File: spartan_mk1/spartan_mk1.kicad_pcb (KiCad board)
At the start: 4 copper layers, 46.5 x 46.5 mm, 90 parts, among them J1 USB_B_Micro, J10 Conn_01x02_Female, J11 Conn_01x02_Female, J12 Conn_01x02_Female, J13 Conn_02x05_Odd_Even, J14 Conn_01x02_Female, J15 Conn_01x08_Female, J18 Conn_01x08_Female, J2 Conn_01x02_Female, J3 Conn_01x02_Female, J4 Conn_01x02_Female, J5 Conn_01x02_Female, J6 Conn_01x02_Female, J8 Conn_01x03_Female, J9 Conn_01x03_Female, Q1 2N7002, Q2 2N7002, Q3 AO3401A, SW1 SW_SPST, U1 MPU-6050, U2 AT24C256C-SSHL-T, U3 USBLC6-2SC6, U4 STM32F405RGTx, U5 AMS1117-3.3, U6 TPS5430DDA, Y1 X322516MLB4SI

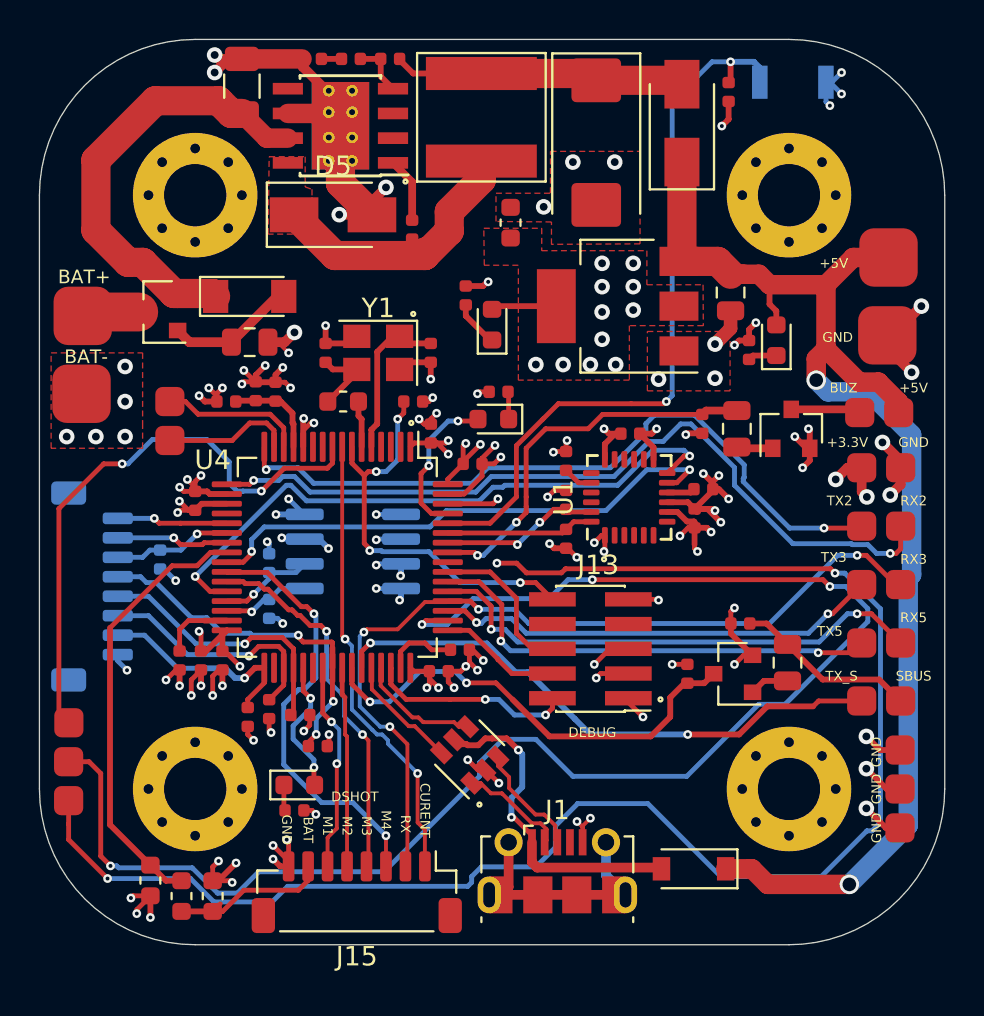
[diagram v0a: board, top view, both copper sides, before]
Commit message: Updated LED labels
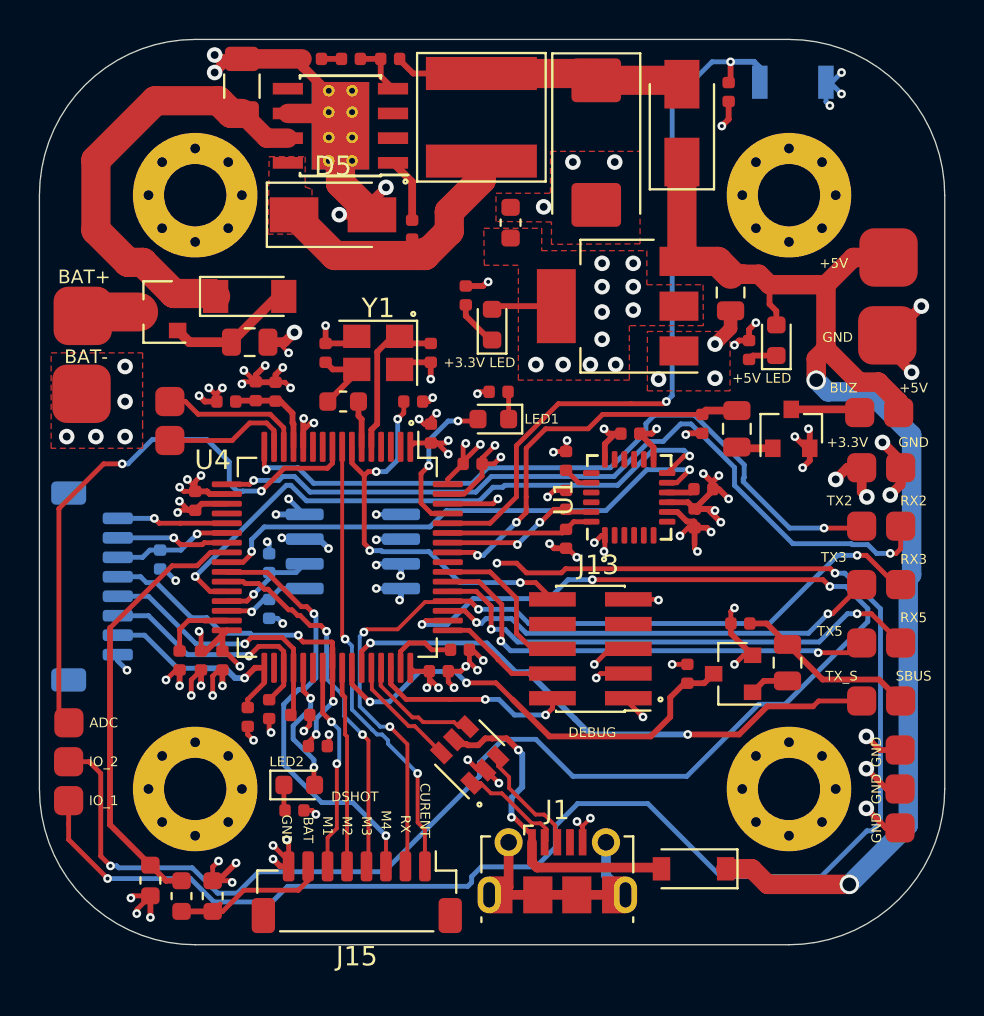
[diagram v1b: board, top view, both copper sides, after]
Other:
- board text added: "+3.3V LED"
- board text added: "+5V LED"
- board text added: "ADC"
- board text added: "IO_1"
- board text added: "IO_2"
- board text added: "LED1"
- board text added: "LED2"
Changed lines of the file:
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@@
   (general
     (thickness 1.6)
-    (drawings 54)
+    (drawings 61)
     (tracks 1230)
     (zones 0)
@@
     (46 B.CrtYd user)
     (47 F.CrtYd user)
-    (48 B.Fab user)
-    (49 F.Fab user)
+    (48 B.Fab user hide)
+    (49 F.Fab user hide)
   )
   (setup
@@
     )
   )
+  (gr_text LED2 (at 64.7 89.1) (layer F.SilkS)
+    (effects (font (size 0.5 0.5) (thickness 0.125)))
+  )
+  (gr_text LED1 (at 77.8 71.5) (layer F.SilkS)
+    (effects (font (size 0.5 0.5) (thickness 0.125)))
+  )
+  (gr_text "+3.3V LED" (at 74.6 68.6) (layer F.SilkS)
+    (effects (font (size 0.5 0.5) (thickness 0.125)))
+  )
+  (gr_text "+5V LED" (at 89.1 69.4) (layer F.SilkS)
+    (effects (font (size 0.5 0.5) (thickness 0.125)))
+  )
+  (gr_text IO_1 (at 55.3 91.1) (layer F.SilkS)
+    (effects (font (size 0.5 0.5) (thickness 0.125)))
+  )
+  (gr_text IO_2 (at 55.3 89.1) (layer F.SilkS)
+    (effects (font (size 0.5 0.5) (thickness 0.125)))
+  )
+  (gr_text ADC (at 55.3 87.1) (layer F.SilkS)
+    (effects (font (size 0.5 0.5) (thickness 0.125)))
+  )
   (gr_circle (center 83.9 85.9) (end 83.9 85.8) (layer F.SilkS) (width 0.12))
   (gr_circle (center 72.1 76.4) (end 72.2 76.4) (layer B.SilkS) (width 0.12))
@@
     (connect_pads (clearance 0.254))
     (min_thickness 0.254)
-    (fill yes (arc_segments 32) (thermal_gap 0.508) (thermal_bridge_width 0.508))
+    (fill (arc_segments 32) (thermal_gap 0.508) (thermal_bridge_width 0.508))
     (polygon
       (pts
@@
     (connect_pads (clearance 0.3))
     (min_thickness 0.254)
-    (fill yes (arc_segments 32) (thermal_gap 0.508) (thermal_bridge_width 0.508))
+    (fill (arc_segments 32) (thermal_gap 0.508) (thermal_bridge_width 0.508))
     (polygon
       (pts
@@
     (connect_pads (clearance 0.3))
     (min_thickness 0.254)
-    (fill yes (arc_segments 32) (thermal_gap 0.3) (thermal_bridge_width 2))
+    (fill (arc_segments 32) (thermal_gap 0.3) (thermal_bridge_width 2))
     (polygon
       (pts
@@
     (connect_pads (clearance 0.3))
     (min_thickness 0.254)
-    (fill yes (arc_segments 32) (thermal_gap 0.5) (thermal_bridge_width 0.5))
+    (fill (arc_segments 32) (thermal_gap 0.5) (thermal_bridge_width 0.5))
     (polygon
       (pts
@@
     (connect_pads (clearance 0.3))
     (min_thickness 0.254)
-    (fill yes (arc_segments 32) (thermal_gap 0.5) (thermal_bridge_width 0.8))
+    (fill (arc_segments 32) (thermal_gap 0.5) (thermal_bridge_width 0.8))
     (polygon
       (pts
@@
     (connect_pads (clearance 0.3))
     (min_thickness 0.254)
-    (fill yes (arc_segments 32) (thermal_gap 0.2) (thermal_bridge_width 0.8))
+    (fill (arc_segments 32) (thermal_gap 0.2) (thermal_bridge_width 0.8))
     (polygon
       (pts
@@
     (connect_pads (clearance 0.3))
     (min_thickness 0.254)
-    (fill yes (arc_segments 32) (thermal_gap 0.2) (thermal_bridge_width 2))
+    (fill (arc_segments 32) (thermal_gap 0.2) (thermal_bridge_width 2))
     (polygon
       (pts

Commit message: Generated gerber files. Positions and BOM assemly files generated
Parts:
- C7, C8: footprint Capacitor_SMD:C_0402_1005Metric -> Capacitor_SMD:C_0603_1608Metric
- R13: footprint Resistor_SMD:R_0603_1608Metric -> Resistor_SMD:R_0402_1005Metric
- moved C14 0.68 mm to (72.0, 84.9), turned to 270 degrees
- moved C8 0.67 mm to (74.1, 83.8)
- moved R13 0.46 mm to (68.0, 70.4)
- moved C7 0.20 mm to (59.0, 83.9)
- renumbered Re to R28
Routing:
- net GND: track 139.8 -> 136.8 mm, vias 101 -> 99
- net +3V3: track 49.9 -> 48.6 mm, vias 44 -> 43
- net Net-(C7-Pad1): track 4.02 -> 3.34 mm
- net /SWDIO: track 10.5 -> 11.1 mm
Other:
- board text added: "JLCJLCJLCJLC"
